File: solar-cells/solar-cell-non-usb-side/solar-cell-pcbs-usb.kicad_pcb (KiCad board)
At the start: 2 copper layers, 80 x 103.5 mm, 22 parts, among them J1 Solar Cell

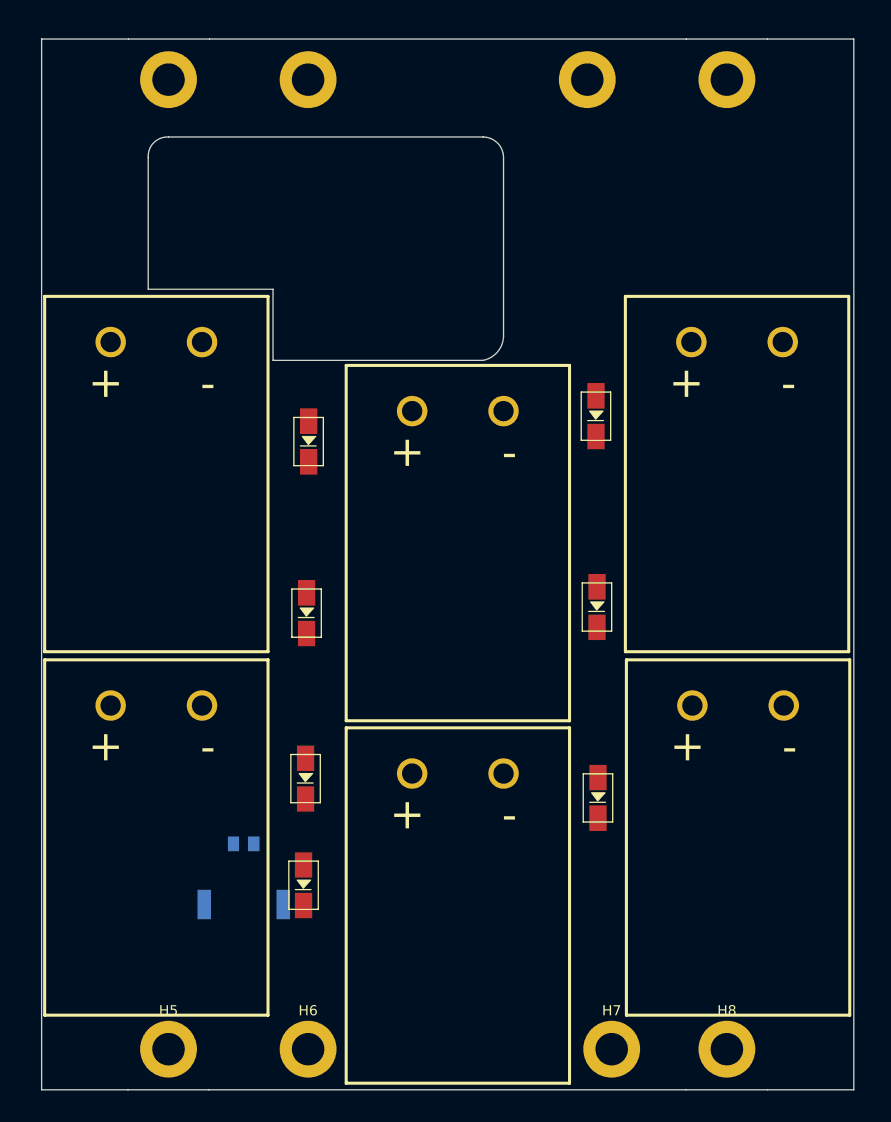
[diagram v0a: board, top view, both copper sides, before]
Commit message: traces added
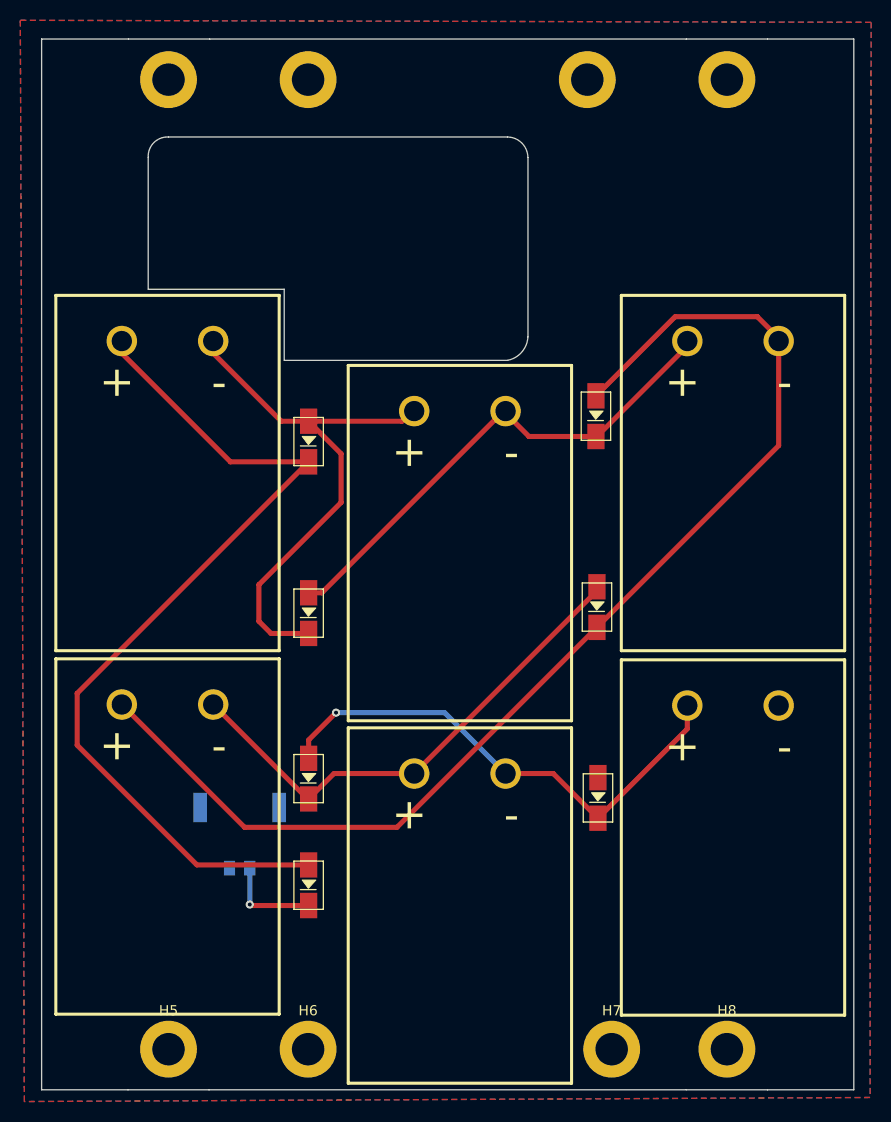
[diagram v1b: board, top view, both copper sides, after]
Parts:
- moved J1 3.39 mm to (90.6, 120.4), turned to 180 degrees
- moved SC4 1.10 mm to (85.0, 117.3)
- moved SC1 1.10 mm to (85.0, 81.5)
- moved D9 0.50 mm to (98.4, 122.1)
- moved SC6 0.50 mm to (140.7, 117.4)
- moved SC3 0.41 mm to (140.7, 81.5)
- moved D5 0.30 mm to (98.4, 111.6)
- moved D2 0.20 mm to (98.4, 95.3)
- moved SC2 0.20 mm to (113.8, 88.4)
- moved SC5 0.20 mm to (113.8, 124.1)
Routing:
- net Net-(D3-Pad2): track 0.00 -> 118.3 mm
- net Net-(D1-Pad1): track 0.00 -> 89.4 mm
- net Net-(D1-Pad2): track 0.00 -> 54.1 mm
- net Net-(D4-Pad2): track 0.00 -> 50.5 mm
- net Net-(D5-Pad2): track 0.00 -> 50.5 mm, vias 0 -> 1
- net Net-(D2-Pad2): track 0.00 -> 50.0 mm
- net VSOLAR: track 0.00 -> 9.42 mm, vias 0 -> 1
- added copper zone on B.Cu, net GND
- added copper zone on F.Cu, net GND
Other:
- outline, holes or cut-outs redrawn

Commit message: added silkscreens
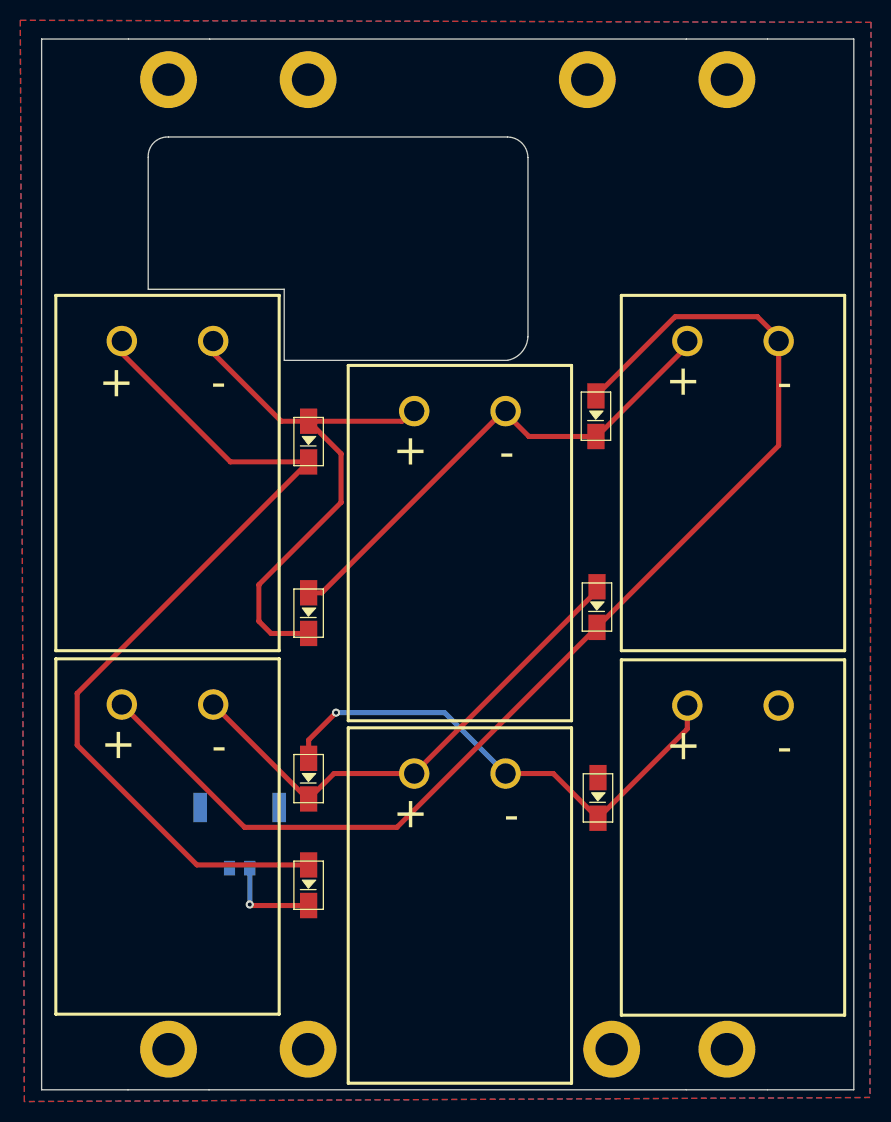
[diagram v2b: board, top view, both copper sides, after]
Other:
- board text added: "+"
- board text added: "-"
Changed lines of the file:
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@@
     (property "Sheetname" "")
     (attr exclude_from_pos_files)
-    (fp_text reference "H7" (at 0 -3.8) (layer "F.SilkS")
+    (fp_text reference "H7" (at 0 -3.8) (layer "F.Fab")
       (effects (font (size 1 1) (thickness 0.15)))
     )
@@
       (effects (font (size 1 1) (thickness 0.15)))
     )
-    (fp_text user "+" (at 8.89 -5.58 90) (layer "F.SilkS")
-      (effects (font (size 3 3) (thickness 0.3)))
-    )
-    (fp_text user "-" (at 8.89 4.58) (layer "F.SilkS")
+    (fp_text user "-" (at 8.92 4.5) (layer "B.SilkS")
+      (effects (font (size 3 3) (thickness 0.3)))
+    )
+    (fp_text user "+" (at 8.85 -5.63 90) (layer "F.SilkS")
       (effects (font (size 3 3) (thickness 0.3)))
     )
@@
       (effects (font (size 1 1) (thickness 0.15)))
     )
-    (fp_text user "+" (at 8.89 -5.58 90) (layer "F.SilkS")
+    (fp_text user "+" (at 8.89 -5.62 90) (layer "B.SilkS")
       (effects (font (size 3 3) (thickness 0.3)))
     )
@@
     (property "Sheetname" "")
     (attr exclude_from_pos_files)
-    (fp_text reference "H8" (at 0 -3.8) (layer "F.SilkS")
+    (fp_text reference "H8" (at 0 -3.8) (layer "F.Fab")
       (effects (font (size 1 1) (thickness 0.15)))
     )
@@
       (effects (font (size 1 1) (thickness 0.15)))
     )
+    (fp_text user "+" (at 8.89 -5.58 90) (layer "B.SilkS")
+      (effects (font (size 3 3) (thickness 0.3)))
+    )
     (fp_text user "-" (at 8.89 4.58) (layer "F.SilkS")
-      (effects (font (size 3 3) (thickness 0.3)))
-    )
-    (fp_text user "+" (at 8.89 -5.58 90) (layer "F.SilkS")
       (effects (font (size 3 3) (thickness 0.3)))
     )
@@
       (effects (font (size 1 1) (thickness 0.15)))
     )
-    (fp_text user "+" (at 8.89 -5.58 90) (layer "F.SilkS")
-      (effects (font (size 3 3) (thickness 0.3)))
-    )
-    (fp_text user "-" (at 8.89 4.58) (layer "F.SilkS")
+    (fp_text user "+" (at 8.9 -5.56 90) (layer "B.SilkS")
       (effects (font (size 3 3) (thickness 0.3)))
     )
@@
     (property "Sheetname" "")
     (attr exclude_from_pos_files)
-    (fp_text reference "H5" (at 0 -3.8) (layer "F.SilkS")
+    (fp_text reference "H5" (at 0 -3.8) (layer "F.Fab")
       (effects (font (size 1 1) (thickness 0.15)))
     )
@@
       (effects (font (size 1 1) (thickness 0.15)))
     )
-    (fp_text user "+" (at 8.89 -5.58 90) (layer "F.SilkS")
+    (fp_text user "+" (at 8.89 -5.56 90) (layer "B.SilkS")
       (effects (font (size 3 3) (thickness 0.3)))
     )
@@
     (property "Sheetname" "")
     (attr exclude_from_pos_files)
-    (fp_text reference "H6" (at 0 -3.8) (layer "F.SilkS")
+    (fp_text reference "H6" (at 0 -3.8) (layer "F.Fab")
       (effects (font (size 1 1) (thickness 0.15)))
     )
@@
       (effects (font (size 1 1) (thickness 0.15)))
     )
+    (fp_text user "+" (at 8.89 -5.58 90) (layer "B.SilkS")
+      (effects (font (size 3 3) (thickness 0.3)))
+    )
     (fp_text user "-" (at 8.89 4.58) (layer "F.SilkS")
-      (effects (font (size 3 3) (thickness 0.3)))
-    )
-    (fp_text user "+" (at 8.89 -5.58 90) (layer "F.SilkS")
       (effects (font (size 3 3) (thickness 0.3)))
     )
@@
     (property "Sheetname" "")
     (attr through_hole)
-    (fp_text reference "J1" (at -1.0285 -4.950001) (layer "B.SilkS")
+    (fp_text reference "J1" (at 6.465 3.78) (layer "B.SilkS")
       (effects (font (size 1 1) (thickness 0.15)) (justify mirror))
     )
@@
   (gr_line (start 72.1 142.25) (end 72.1 38.75) (layer "Edge.Cuts") (width 0.1))
   (gr_line (start 96 63.4) (end 82.6 63.4) (layer "Edge.Cuts") (width 0.1))
+  (gr_text "-\n" (at 90.62 125.72) (layer "B.SilkS")
+    (effects (font (size 1 1) (thickness 0.15)) (justify mirror))
+  )
+  (gr_text "-" (at 89.59 108.41) (layer "B.SilkS")
+    (effects (font (size 3 3) (thickness 0.3)))
+  )
+  (gr_text "+" (at 92.32 125.7) (layer "B.SilkS")
+    (effects (font (size 1 1) (thickness 0.15)) (justify mirror))
+  )
+  (gr_text "-" (at 117.94 79.48) (layer "B.SilkS")
+    (effects (font (size 3 3) (thickness 0.3)))
+  )
+  (gr_text "-" (at 118.39 115.2) (layer "B.SilkS")
+    (effects (font (size 3 3) (thickness 0.3)))
+  )
+  (gr_text "-" (at 145.28 73.05 180) (layer "B.SilkS")
+    (effects (font (size 3 3) (thickness 0.3)))
+  )
+  (gr_text "+" (at 79.63 72.42) (layer "B.SilkS")
+    (effects (font (size 3 3) (thickness 0.3)))
+  )
+  (gr_text "-" (at 145.28 108.52) (layer "B.SilkS")
+    (effects (font (size 3 3) (thickness 0.3)))
+  )
+  (gr_text "+" (at 135.32 108.3) (layer "F.SilkS")
+    (effects (font (size 3 3) (thickness 0.3)))
+  )
+  (gr_text "+" (at 135.29 72.4) (layer "F.SilkS")
+    (effects (font (size 3 3) (thickness 0.3)))
+  )
+  (gr_text "-" (at 89.53 72.58) (layer "F.SilkS")
+    (effects (font (size 3 3) (thickness 0.3)))
+  )
+  (gr_text "-" (at 117.92 79.47) (layer "F.SilkS")
+    (effects (font (size 3 3) (thickness 0.3)))
+  )
+  (gr_text "+" (at 79.66 108.19) (layer "F.SilkS")
+    (effects (font (size 3 3) (thickness 0.3)))
+  )
+  (gr_text "+" (at 108.44 115) (layer "F.SilkS")
+    (effects (font (size 3 3) (thickness 0.3)))
+  )
+  (gr_text "+" (at 108.43 79.27) (layer "F.SilkS")
+    (effects (font (size 3 3) (thickness 0.3)))
+  )
   (dimension (type aligned) (layer "Dwgs.User")
     (pts (xy 98.35 138.25) (xy 98.25 124.025))

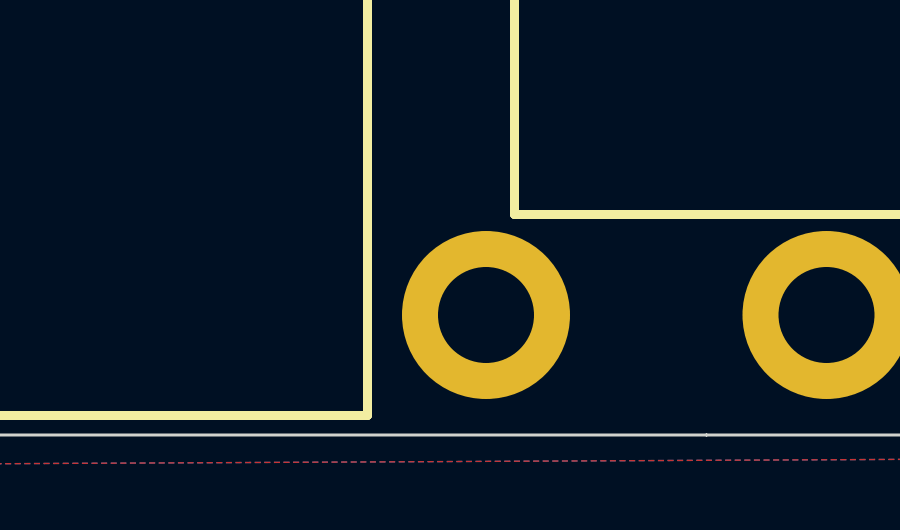
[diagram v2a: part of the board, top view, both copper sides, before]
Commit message: fixed mounting holes
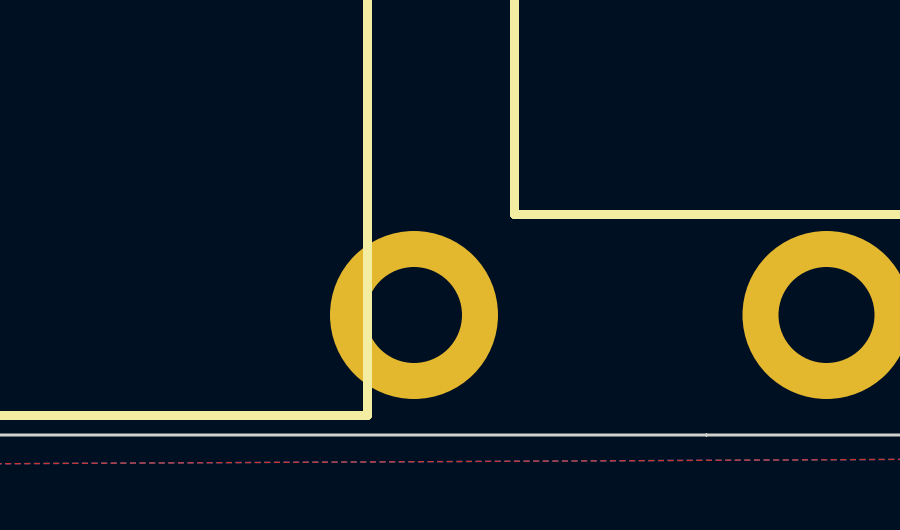
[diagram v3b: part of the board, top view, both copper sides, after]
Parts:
- moved H7 2.40 mm to (125.8, 138.2)
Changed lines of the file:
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@@
   (net 8 "VSOLAR")
   (footprint "MountingHole:MountingHole_3.2mm_M3_DIN965_Pad" (layer "F.Cu")
-    (at 128.25 138.25)
+    (at 125.85 138.25)
     (descr "Mounting Hole 3.2mm, M3, DIN965")
     (tags "mounting hole 3.2mm m3 din965")
@@
     (property "Sheetname" "")
     (attr through_hole)
-    (fp_text reference "J1" (at 6.465 3.78) (layer "B.SilkS")
+    (fp_text reference "J1" (at 6.465 3.78) (layer "B.Fab")
       (effects (font (size 1 1) (thickness 0.15)) (justify mirror))
     )
-    (fp_text value "Solar Cell" (at -0.9535 9.874999) (layer "B.SilkS")
+    (fp_text value "Solar Cell" (at -7.475 3.34 270) (layer "B.SilkS")
       (effects (font (size 1 1) (thickness 0.15)) (justify mirror))
     )
@@
   )
   (dimension (type aligned) (layer "Dwgs.User")
-    (pts (xy 79.6 135) (xy 79.6 112.7))
-    (height -9.8)
-    (gr_text "22.3000 mm" (at 68 123.85 90) (layer "Dwgs.User")
-      (effects (font (size 1.5 1.5) (thickness 0.3)))
-    )
-    (format (units 3) (units_format 1) (precision 4))
-    (style (thickness 0.2) (arrow_length 1.27) (text_position_mode 0) (extension_height 0.58642) (extension_offset 0.5) keep_text_aligned)
+    (pts (xy 98.35 138.25) (xy 125.85 138.25))
+    (height 23.25)
+    (gr_text "27.5000 mm" (at 112.1 160.35) (layer "Dwgs.User")
+      (effects (font (size 1 1) (thickness 0.15)))
+    )
+    (format (units 3) (units_format 1) (precision 4))
+    (style (thickness 0.15) (arrow_length 1.27) (text_position_mode 0) (extension_height 0.58642) (extension_offset 0.5) keep_text_aligned)
+  )
+  (dimension (type aligned) (layer "Dwgs.User")
+    (pts (xy 125.85 42.75) (xy 139.6 42.75))
+    (height -14.65)
+    (gr_text "13.7500 mm" (at 132.725 26.95) (layer "Dwgs.User")
+      (effects (font (size 1 1) (thickness 0.15)))
+    )
+    (format (units 3) (units_format 1) (precision 4))
+    (style (thickness 0.15) (arrow_length 1.27) (text_position_mode 0) (extension_height 0.58642) (extension_offset 0.5) keep_text_aligned)
+  )
+  (dimension (type aligned) (layer "Dwgs.User")
+    (pts (xy 125.85 138.25) (xy 139.6 138.25))
+    (height 16.85)
+    (gr_text "13.7500 mm" (at 132.725 153.95) (layer "Dwgs.User")
+      (effects (font (size 1 1) (thickness 0.15)))
+    )
+    (format (units 3) (units_format 1) (precision 4))
+    (style (thickness 0.15) (arrow_length 1.27) (text_position_mode 0) (extension_height 0.58642) (extension_offset 0.5) keep_text_aligned)
   )
   (dimension (type aligned) (layer "Dwgs.User")
@@
     (height -10.15)
     (gr_text "27.5000 mm" (at 112.1 31.45) (layer "Dwgs.User")
+      (effects (font (size 1 1) (thickness 0.15)))
+    )
+    (format (units 3) (units_format 1) (precision 4))
+    (style (thickness 0.15) (arrow_length 1.27) (text_position_mode 0) (extension_height 0.58642) (extension_offset 0.5) keep_text_aligned)
+  )
+  (dimension (type aligned) (layer "Dwgs.User")
+    (pts (xy 84.6 138.25) (xy 98.35 138.25))
+    (height 18.45)
+    (gr_text "13.7500 mm" (at 91.475 155.55) (layer "Dwgs.User")
       (effects (font (size 1 1) (thickness 0.15)))
     )
@@
   )
   (dimension (type aligned) (layer "Dwgs.User")
-    (pts (xy 76 53.25) (xy 76 48.25))
-    (height -6.5)
-    (gr_text "5.0000 mm" (at 67.7 50.75 90) (layer "Dwgs.User")
-      (effects (font (size 1.5 1.5) (thickness 0.3)))
-    )
-    (format (units 3) (units_format 1) (precision 4))
-    (style (thickness 0.2) (arrow_length 1.27) (text_position_mode 0) (extension_height 0.58642) (extension_offset 0.5) keep_text_aligned)
-  )
-  (dimension (type aligned) (layer "Dwgs.User")
-    (pts (xy 82.6 110.95) (xy 82.6 114.45))
-    (height 21.85)
-    (gr_text "3.5000 mm" (at 58.95 112.7 90) (layer "Dwgs.User")
-      (effects (font (size 1.5 1.5) (thickness 0.3)))
-    )
-    (format (units 3) (units_format 1) (precision 4))
-    (style (thickness 0.2) (arrow_length 1.27) (text_position_mode 0) (extension_height 0.58642) (extension_offset 0.5) keep_text_aligned)
-  )
-  (dimension (type aligned) (layer "Dwgs.User")
     (pts (xy 72.1 38.75) (xy 72.1 142.25))
     (height 17.849999)
@@
       (effects (font (size 1.5 1.5) (thickness 0.3)))
     )
-    (format (units 3) (units_format 1) (precision 4))
-    (style (thickness 0.2) (arrow_length 1.27) (text_position_mode 0) (extension_height 0.58642) (extension_offset 0.5) keep_text_aligned)
-  )
-  (dimension (type aligned) (layer "Dwgs.User")
-    (pts (xy 82.6 112.7) (xy 82.6 68.3))
-    (height -16.85)
-    (gr_text "44.4000 mm" (at 63.95 90.5 90) (layer "Dwgs.User")
-      (effects (font (size 1.5 1.5) (thickness 0.3)))
-    )
